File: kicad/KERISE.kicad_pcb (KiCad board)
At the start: 2 copper layers, 46 x 50 mm, 144 parts, among them J1 COM, P1 ANT, P10 Partition, P11 PR_Host, P12 PR_Slave, P13 Partition, P14 Partition, P15 Partition, P16 Partition, P17 Fan, P18 ENC_Host, P19 ENC_Slave, P2 Motor_L, P20 ToF_Host, P21 ToF_Slave, P22 ENC_Host, P23 ENC_Slave, P24 PR_Host, P25 PR_Slave, P26 Partition, P27 Partition, P28 Partition, P29 Partition, P3 Motor_R, P30 PR_Host, P31 PR_Slave, P32 Partition, P33 Partition, P34 Partition, P35 Partition, P4 Battery, P5 PR_Host, P6 PR_Slave, P7 Partition, P8 Partition, P9 Partition, Q1 DMN3065LW-7, Q2 DMN3065LW-7, Q3 NX3020NAKW, Q4 DMN3065LW-7, Q5 DMN3065LW-7, Q6 DMN3065LW-7, SW1 SW_Push, SW2 SW_Push, U1 FLASH, U10 AS5048A, U11 ICM-20602, U12 AD8601, U13 AD8601, U2 ESP32, U3 XTAL, U4 DRV8835, U5 LXDC2URxx, U6 AD8601, U7 AD8601, U8 AS5048A, U9 VL53L0X

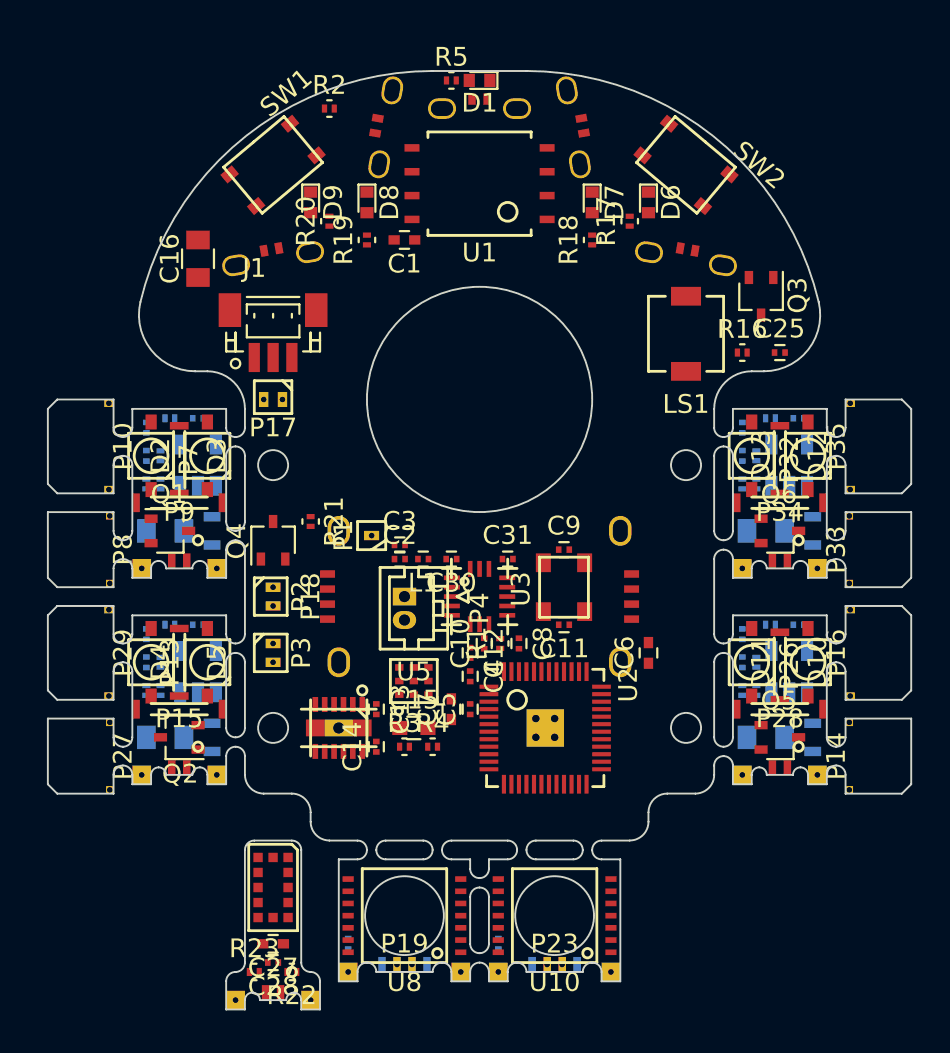
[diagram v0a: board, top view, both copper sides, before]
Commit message: 部品を配置
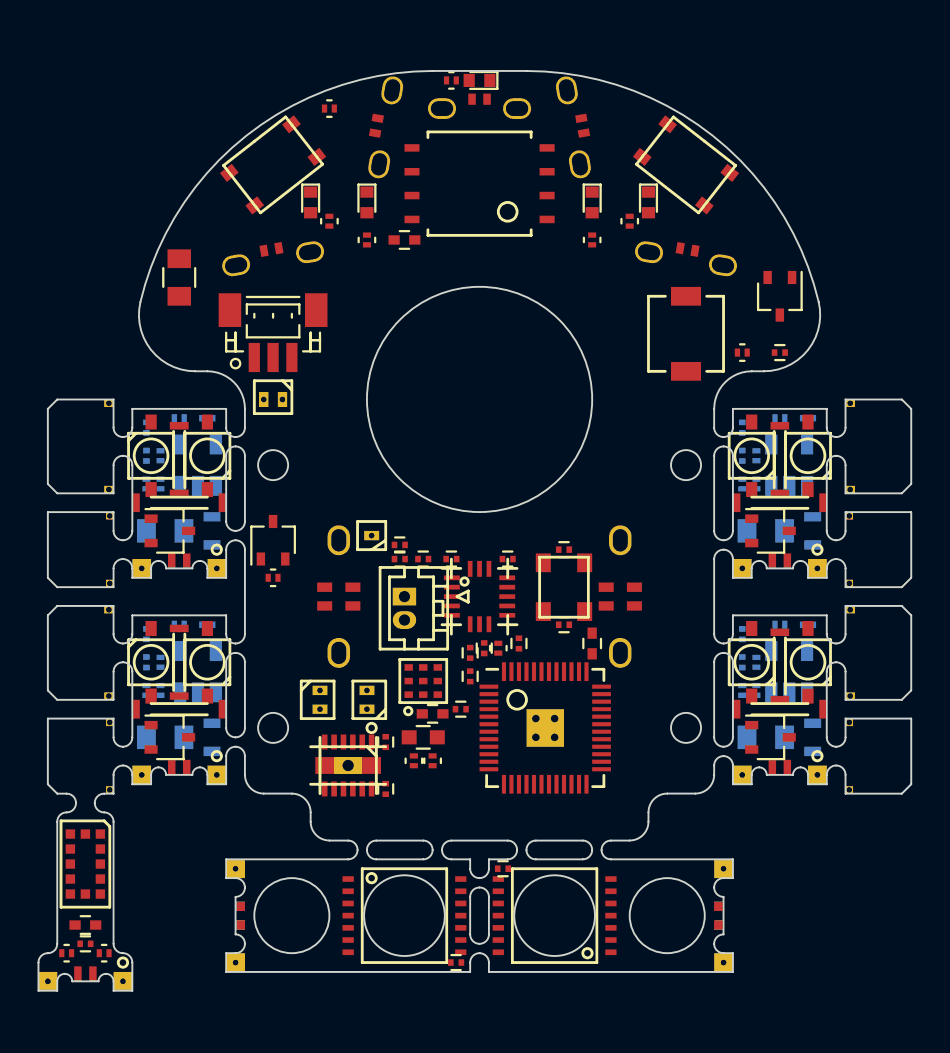
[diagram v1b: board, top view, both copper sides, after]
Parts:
- C26, C29: moved to F.Cu
- moved U9 10.1 mm to (127.5, 127.2)
- moved C27 10.0 mm to (127.5, 130.5)
- moved C28 10.0 mm to (127.5, 131.5)
- moved P21 10.0 mm to (127.5, 133.5)
- moved R22 10.0 mm to (128.5, 132.0)
- moved R23 10.0 mm to (126.5, 132.0)
- moved P19 9.49 mm to (135.5, 130.0), turned to 270 degrees
- moved P23 9.49 mm to (161.5, 130.0), turned to 90 degrees
- moved P2 7.43 mm to (142.5, 118.5), turned to 90 degrees
- moved C26 5.84 mm to (147.2, 132.5), turned to 0 degrees
- moved C29 4.01 mm to (149.8, 127.5), turned to 180 degrees
- moved R21 3.61 mm to (137.5, 112.0), turned to 0 degrees
- moved P3 3.54 mm to (140.0, 118.5)
- moved C6 3.04 mm to (154.5, 115.5), turned to 270 degrees
- moved C14 2.30 mm to (143.5, 123.2)
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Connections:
- P18 pad 2: SPI-CS-ENC -> SPI-MOSI
- P18 pad 3: SPI-SCLK -> ENC-CHAIN
- P18 pad 4: ENC-CHAIN -> SPI-SCLK
- P18 pad 5: SPI-MOSI -> SPI-CS-ENC
- P19 pad 2: /Encoder_R/s_CS -> /Encoder_R/s_MOSI
- P19 pad 3: /Encoder_R/s_SCLK -> /Encoder_R/s_MISO
- P19 pad 4: /Encoder_R/s_MISO -> /Encoder_R/s_SCLK
- P19 pad 5: /Encoder_R/s_MOSI -> /Encoder_R/s_CS
- P22 pad 2: SPI-CS-ENC -> ENC-CHAIN
- P22 pad 3: SPI-SCLK -> SPI-MISO
- P22 pad 4: SPI-MISO -> SPI-SCLK
- P22 pad 5: ENC-CHAIN -> SPI-CS-ENC
- P23 pad 2: /Encoder_L/s_CS -> /Encoder_L/s_MOSI
- P23 pad 3: /Encoder_L/s_SCLK -> /Encoder_L/s_MISO
- P23 pad 4: /Encoder_L/s_MISO -> /Encoder_L/s_SCLK
- P23 pad 5: /Encoder_L/s_MOSI -> /Encoder_L/s_CS
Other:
- board size 46 x 50 mm -> 46.5 x 49 mm
- net class 3.3V: clearance 0.16 -> 0.15; trace_width 0.238 -> 0.23
- net class BATT: clearance 0.16 -> 0.15; via_dia 0.38 -> 0.36
- net class Default: clearance 0.16 -> 0.15; trace_width 0.16 -> 0.15; via_dia 0.34 -> 0.36
- net class GND: clearance 0.16 -> 0.15; via_dia 0.38 -> 0.36
- net class LED: clearance 0.16 -> 0.15
- net class Motor: clearance 0.16 -> 0.15; trace_width 0.3 -> 0.32; via_drill 0.3 -> 0.32
- rule trace_clearance: 0.16 -> 0.15
- rule trace_min: 0.16 -> 0.15
- rule via_min_size: 0.34 -> 0.36

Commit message: 4輪改良版自動配線完了
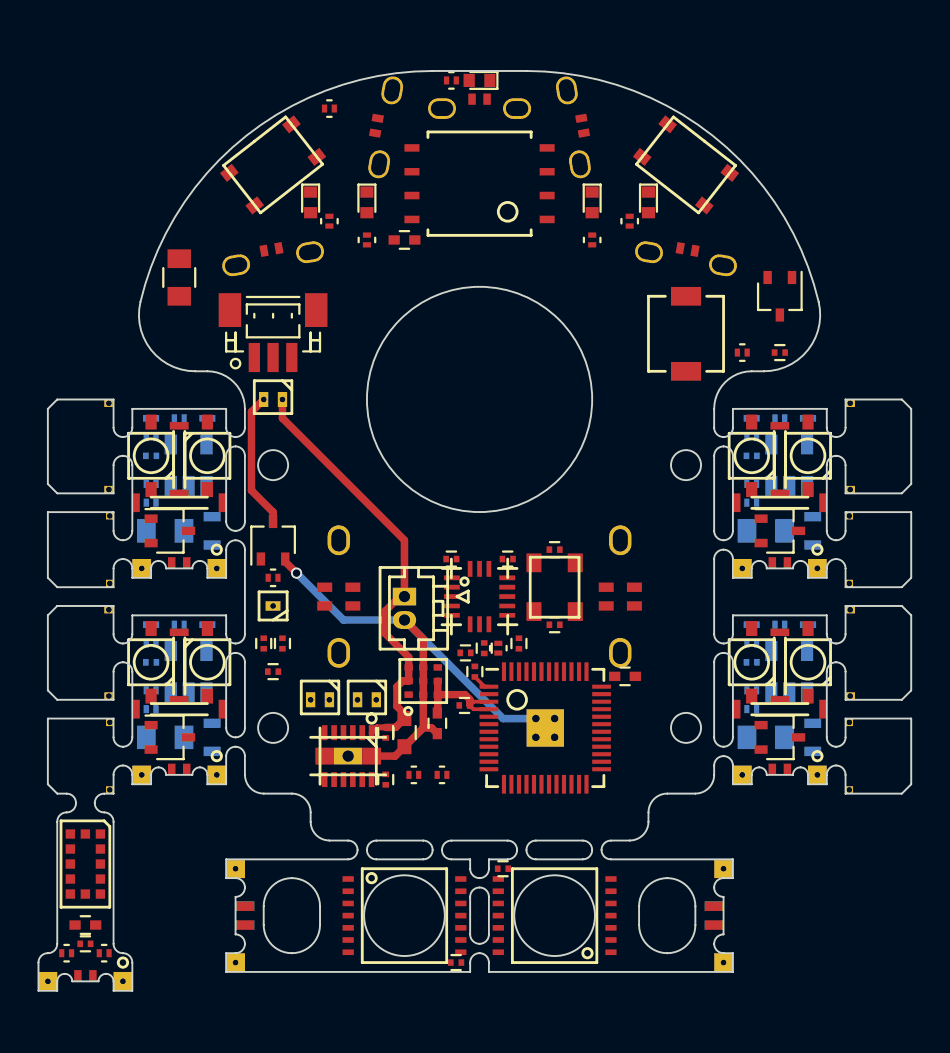
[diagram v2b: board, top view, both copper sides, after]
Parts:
- moved L1 10.0 mm to (137.5, 117.0)
- moved C2 8.53 mm to (137.0, 115.5), turned to 270 degrees
- moved C3 8.16 mm to (138.0, 115.5), turned to 270 degrees
- moved P1 6.45 mm to (137.5, 113.5)
- moved C6 2.47 mm to (156.2, 117.2), turned to 180 degrees
- moved R3 1.68 mm to (146.5, 122.5), turned to 0 degrees
- moved R4 1.25 mm to (145.0, 122.5), turned to 180 degrees
- moved R10 1.12 mm to (131.0, 104.5), turned to 0 degrees
- moved R14 1.12 mm to (131.0, 119.0), turned to 180 degrees
- moved R15 1.12 mm to (131.0, 115.5), turned to 0 degrees
- moved R9 1.12 mm to (131.0, 108.0), turned to 180 degrees
- moved C15 1.03 mm to (144.5, 120.2), turned to 270 degrees
- moved R27 1.03 mm to (163.0, 119.0), turned to 180 degrees
- moved R28 1.03 mm to (163.0, 115.5), turned to 0 degrees
- moved R32 1.03 mm to (163.0, 108.0), turned to 180 degrees
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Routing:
- net GND: track 0.00 -> 27.4 mm, vias 0 -> 1
- net +BATT: track 0.00 -> 23.4 mm
- net /Fan/fan_to_fet: track 0.00 -> 7.25 mm
- net +3V3: track 0.00 -> 7.01 mm
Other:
- outline, holes or cut-outs redrawn
- net class 3.3V: trace_width 0.23 -> 0.24
- net class BATT: trace_width 0.32 -> 0.24; via_drill 0.32 -> 0.3
- net class GND: trace_width 0.32 -> 0.24; via_drill 0.32 -> 0.3
- net class Motor: via_drill 0.32 -> 0.3

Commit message: 細部を改良，自動配線成功
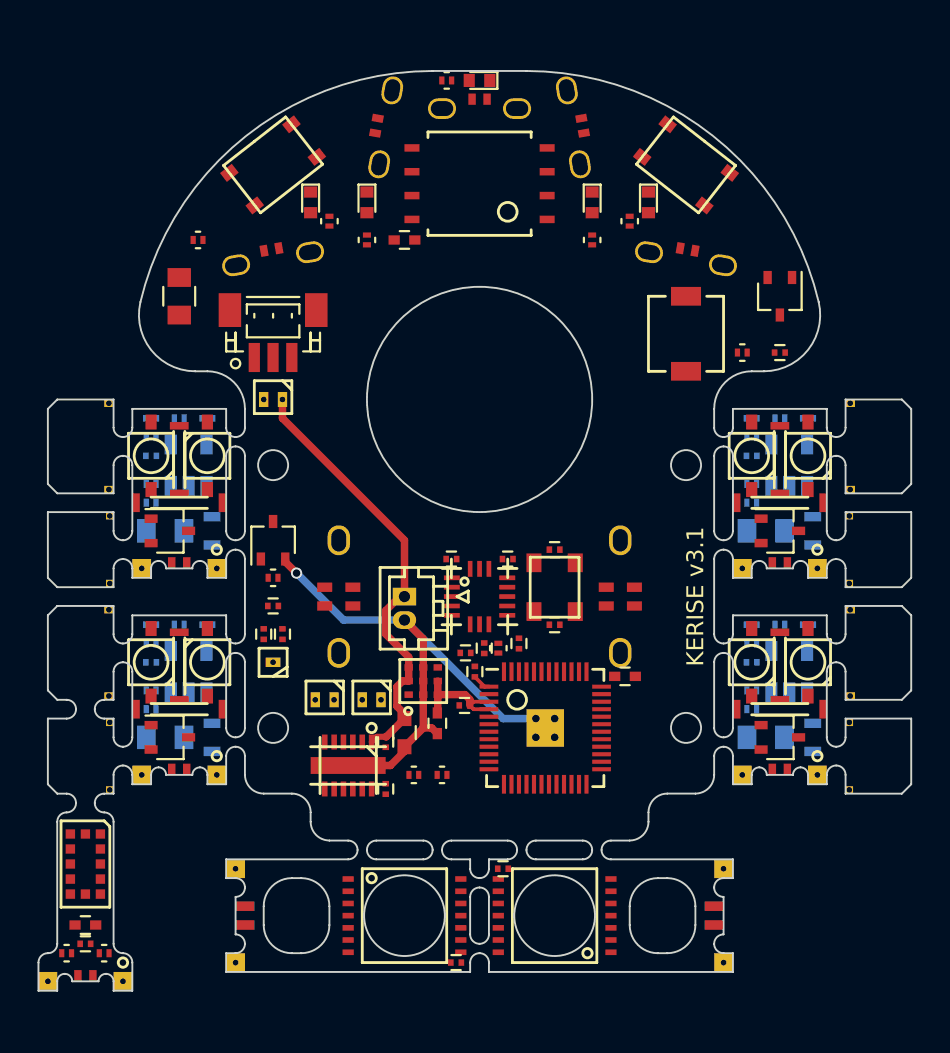
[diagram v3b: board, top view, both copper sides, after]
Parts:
- added G***: LOGO, mouse:KERI_9mm, B.Cu at (148.5, 90.5)
- moved R2 9.90 mm to (133.5, 94.0), turned to 180 degrees
- moved L1 3.50 mm to (137.5, 113.5)
- moved P1 3.00 mm to (137.5, 116.5)
- moved C16 1.00 mm to (132.5, 97.0), turned to 270 degrees
- moved C13 0.50 mm to (143.5, 120.8)
- moved C14 0.50 mm to (143.5, 123.2)
- moved C2 0.50 mm to (137.0, 115.0), turned to 90 degrees
- moved C3 0.50 mm to (138.0, 115.0), turned to 90 degrees
- moved U4 0.50 mm to (141.5, 122.0)
- moved P2 0.25 mm to (142.8, 118.5)
- moved P3 0.25 mm to (140.2, 118.5)
- moved R5 0.25 mm to (146.8, 85.5)
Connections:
- P18 pad 2: SPI-MOSI -> SPI-CS-ENC
- P18 pad 3: ENC-CHAIN -> SPI-SCLK
- P18 pad 4: SPI-SCLK -> SPI-MOSI
- P18 pad 5: SPI-CS-ENC -> ENC-CHAIN
- P19 pad 2: /Encoder_R/s_MOSI -> /Encoder_R/s_CS
- P19 pad 3: /Encoder_R/s_MISO -> /Encoder_R/s_SCLK
- P19 pad 4: /Encoder_R/s_SCLK -> /Encoder_R/s_MOSI
- P19 pad 5: /Encoder_R/s_CS -> /Encoder_R/s_MISO
- P22 pad 2: ENC-CHAIN -> SPI-CS-ENC
- P22 pad 3: SPI-MISO -> SPI-SCLK
- P22 pad 4: SPI-SCLK -> ENC-CHAIN
- P22 pad 5: SPI-CS-ENC -> SPI-MISO
- P23 pad 2: /Encoder_L/s_MOSI -> /Encoder_L/s_CS
- P23 pad 3: /Encoder_L/s_MISO -> /Encoder_L/s_SCLK
- P23 pad 4: /Encoder_L/s_SCLK -> /Encoder_L/s_MOSI
- P23 pad 5: /Encoder_L/s_CS -> /Encoder_L/s_MISO
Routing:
- net /Fan/fan_to_fet: track 7.25 -> 0.00 mm
- net GND: track 27.4 -> 29.0 mm
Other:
- outline, holes or cut-outs redrawn
- net class Analog added: clearance 0.15, trace_width 0.18, via_dia 0.36, via_drill 0.3
- net class BATT: trace_width 0.24 -> 0.2
- board text added: "KERISE v3.1"

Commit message: Elecrowからのリジェクトを修正
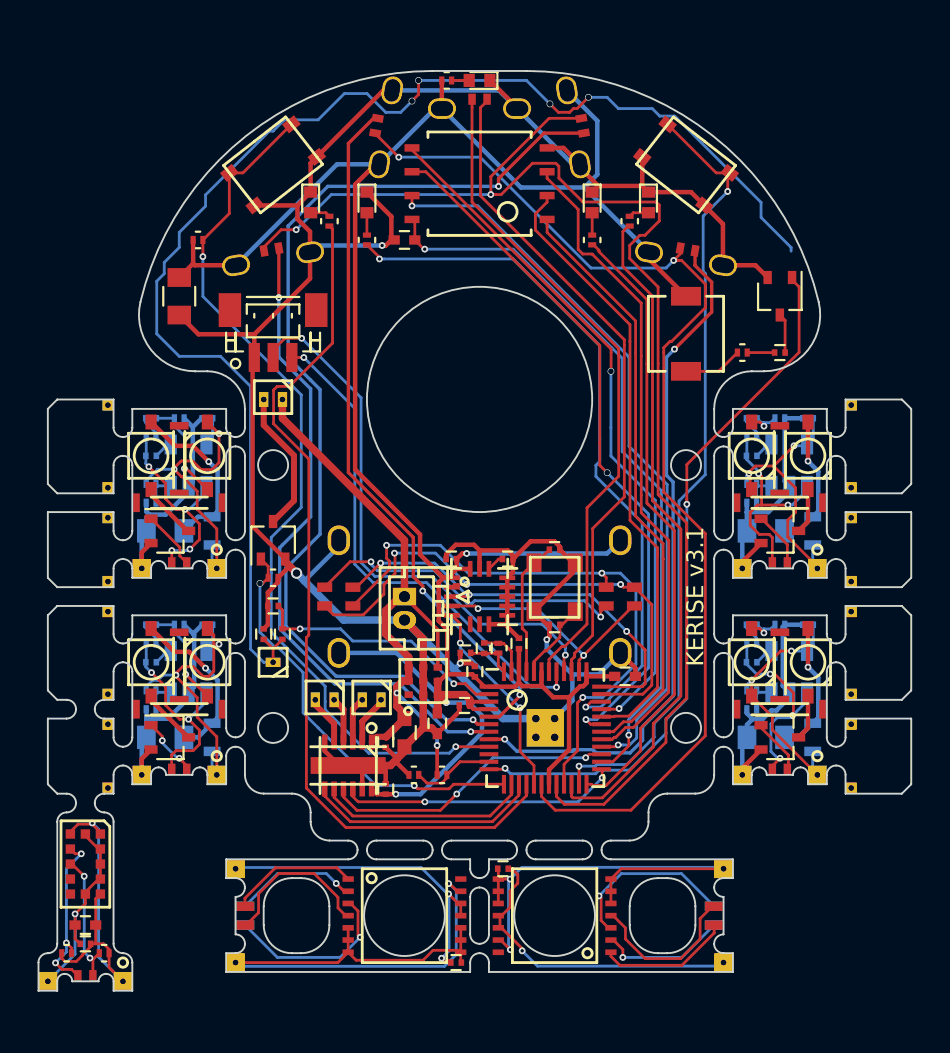
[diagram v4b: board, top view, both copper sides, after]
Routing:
- net GND: track 29.0 -> 155.2 mm, vias 1 -> 4
- net +3V3: track 7.01 -> 128.2 mm, vias 0 -> 3
- net Net-(C2-Pad1): track 0.00 -> 72.3 mm, vias 0 -> 4
- net PR-LED-SR: track 0.00 -> 70.6 mm, vias 0 -> 2
- net PR-LED-SL: track 0.00 -> 59.3 mm, vias 0 -> 2
- net PR-RCV-SR: track 0.00 -> 53.8 mm, vias 0 -> 2
- net Net-(R2-Pad1): track 0.00 -> 47.4 mm, vias 0 -> 2
- net LED_4: track 0.00 -> 46.4 mm
- net BUTTON: track 0.00 -> 41.8 mm, vias 0 -> 2
- net SHD/SD2: track 0.00 -> 39.3 mm, vias 0 -> 2
- net VDD_SDIO: track 0.00 -> 38.9 mm, vias 0 -> 2
- net SPEAKER: track 0.00 -> 37.8 mm, vias 0 -> 2
- net LED_3: track 0.00 -> 37.7 mm, vias 0 -> 2
- net SCK/CLK: track 0.00 -> 37.7 mm, vias 0 -> 2
- net PR-RCV-SL: track 0.00 -> 37.4 mm, vias 0 -> 2
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
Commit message: 部品を配置
壁センサだけ自動配線
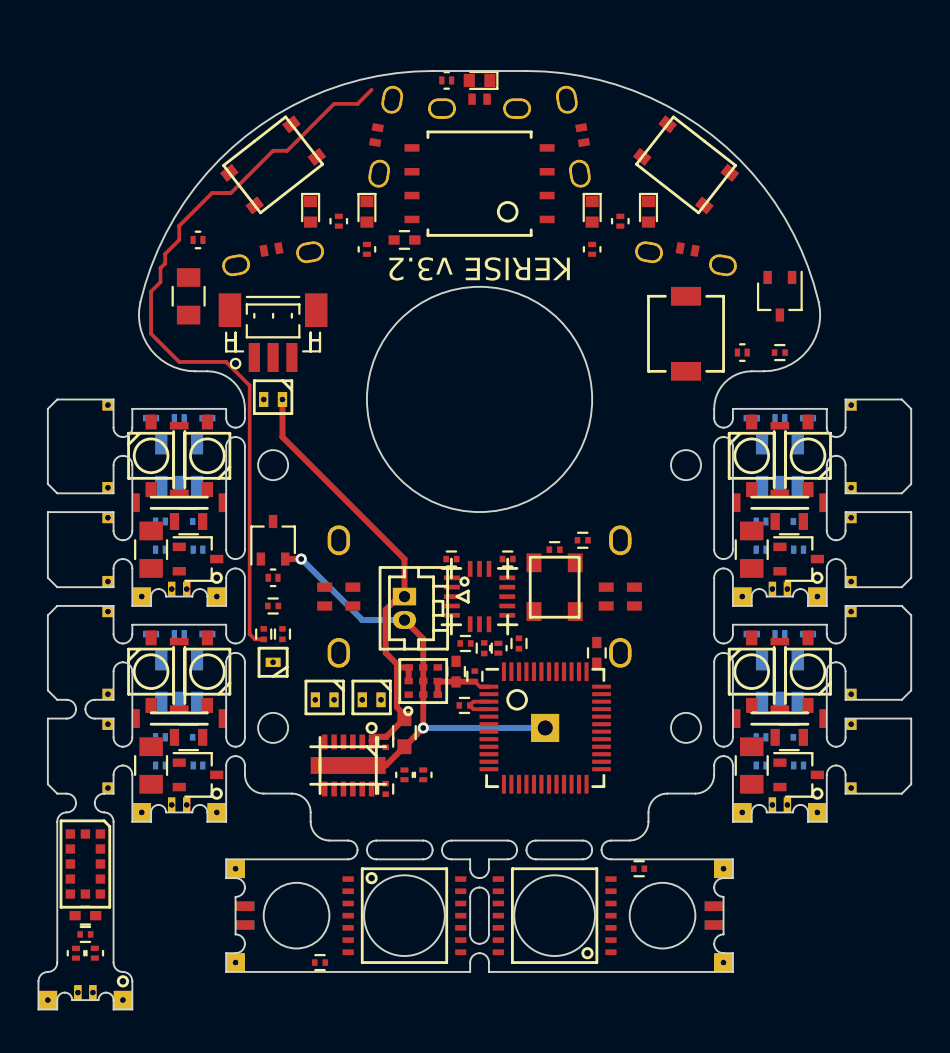
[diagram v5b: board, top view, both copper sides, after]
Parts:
- C17, C21, C32, C36, R11, R24, R29, R6: moved to F.Cu
- moved C26 7.25 mm to (140.0, 132.5), turned to 180 degrees
- moved C29 7.25 mm to (157.0, 127.5), turned to 0 degrees
- moved R15 6.96 mm to (133.5, 122.0)
- moved R28 6.96 mm to (165.5, 122.0)
- moved R10 6.50 mm to (133.5, 110.5)
- moved R33 6.50 mm to (165.5, 110.5)
- moved C11 4.74 mm to (154.0, 110.0)
- moved C23 4.72 mm to (133.5, 120.5)
- moved C34 4.72 mm to (165.5, 120.5)
- moved C19 4.30 mm to (133.5, 109.0)
- moved C38 4.30 mm to (165.5, 109.0)
- moved R13 4.03 mm to (131.5, 122.0), turned to 180 degrees
- moved R26 4.03 mm to (163.5, 122.0), turned to 180 degrees
- moved R31 3.54 mm to (163.5, 110.5), turned to 180 degrees
- moved R8 3.54 mm to (131.5, 110.5), turned to 180 degrees
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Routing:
- net GND: track 155.2 -> 25.2 mm, vias 4 -> 2
- net +3V3: track 128.2 -> 6.01 mm, vias 3 -> 0
- net PR-LED-SR: track 70.6 -> 0.00 mm, vias 2 -> 0
- net PR-LED-SL: track 59.3 -> 0.00 mm, vias 2 -> 0
- net PR-RCV-SR: track 53.8 -> 0.00 mm, vias 2 -> 0
- net Net-(R2-Pad1): track 47.4 -> 0.00 mm, vias 2 -> 0
- net LED_4: track 46.4 -> 0.00 mm
- net BUTTON: track 41.8 -> 0.00 mm, vias 2 -> 0
- net SHD/SD2: track 39.3 -> 0.00 mm, vias 2 -> 0
- net VDD_SDIO: track 38.9 -> 0.00 mm, vias 2 -> 0
- net SPEAKER: track 37.8 -> 0.00 mm, vias 2 -> 0
- net LED_3: track 37.7 -> 0.00 mm, vias 2 -> 0
- net SCK/CLK: track 37.7 -> 0.00 mm, vias 2 -> 0
- net PR-RCV-SL: track 37.4 -> 0.00 mm, vias 2 -> 0
- net PR-RCV-FR: track 37.1 -> 0.00 mm, vias 2 -> 0
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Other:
- board size 46.5 x 49 mm -> 46.5 x 50 mm
- net class 3.3V: trace_width 0.24 -> 0.15; via_dia 0.36 -> 0.5
- net class Analog: trace_width 0.18 -> 0.15; via_dia 0.36 -> 0.5
- net class Antena added: clearance 0.18, trace_width 0.18, via_dia 0.5, via_drill 0.3
- net class BATT: trace_width 0.2 -> 0.15; via_dia 0.36 -> 0.5
- net class Default: via_dia 0.36 -> 0.5
- net class GND: trace_width 0.24 -> 0.15; via_dia 0.36 -> 0.5
- net class LED: via_dia 0.36 -> 0.5
- net class Motor: via_dia 0.36 -> 0.5
- rule via_min_size: 0.36 -> 0.5
- board text added: "KERISE v3.2"
- board text removed: "KERISE v3.1"

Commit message: 配線完了
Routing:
- net GND: track 25.2 -> 155.0 mm, vias 2 -> 4
- net +3V3: track 6.01 -> 127.3 mm, vias 0 -> 2
- net PR-LED-SL: track 0.00 -> 65.5 mm, vias 0 -> 3
- net PR-LED-SR: track 0.00 -> 64.7 mm, vias 0 -> 3
- net Net-(R2-Pad1): track 0.00 -> 50.7 mm, vias 0 -> 3
- net PR-RCV-SR: track 0.00 -> 48.3 mm, vias 0 -> 2
- net LED_4: track 0.00 -> 45.1 mm, vias 0 -> 2
- net VDD_SDIO: track 0.00 -> 42.2 mm, vias 0 -> 2
- net BUTTON: track 0.00 -> 42.1 mm, vias 0 -> 2
- net SHD/SD2: track 0.00 -> 40.1 mm, vias 0 -> 2
- net SCK/CLK: track 0.00 -> 39.5 mm, vias 0 -> 2
- net SPEAKER: track 0.00 -> 39.0 mm, vias 0 -> 2
- net SDI/SD1: track 0.00 -> 37.7 mm
- net I2C-SDA: track 0.00 -> 37.6 mm, vias 0 -> 2
- net UART-RX: track 0.00 -> 37.1 mm, vias 0 -> 2
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
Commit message: 細部の修正
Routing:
- net BUTTON: track 42.1 -> 43.1 mm
- net Net-(R2-Pad1): track 50.7 -> 51.6 mm
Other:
- outline, holes or cut-outs redrawn
